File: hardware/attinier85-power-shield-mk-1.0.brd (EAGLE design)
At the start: 36 x 25 mm, 6 parts, among them Q1 2N7000, U1 ATTINIEST85_SHIELD

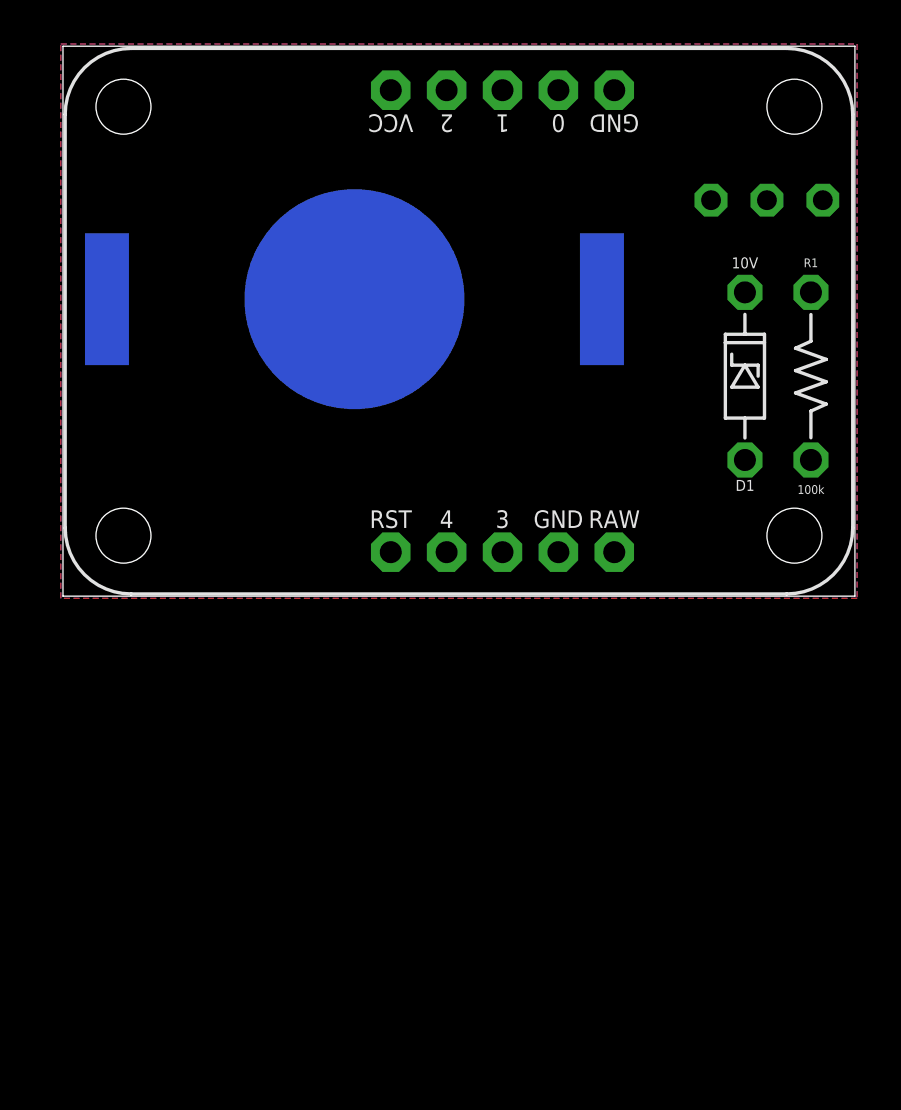
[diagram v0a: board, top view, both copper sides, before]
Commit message: renaming parts
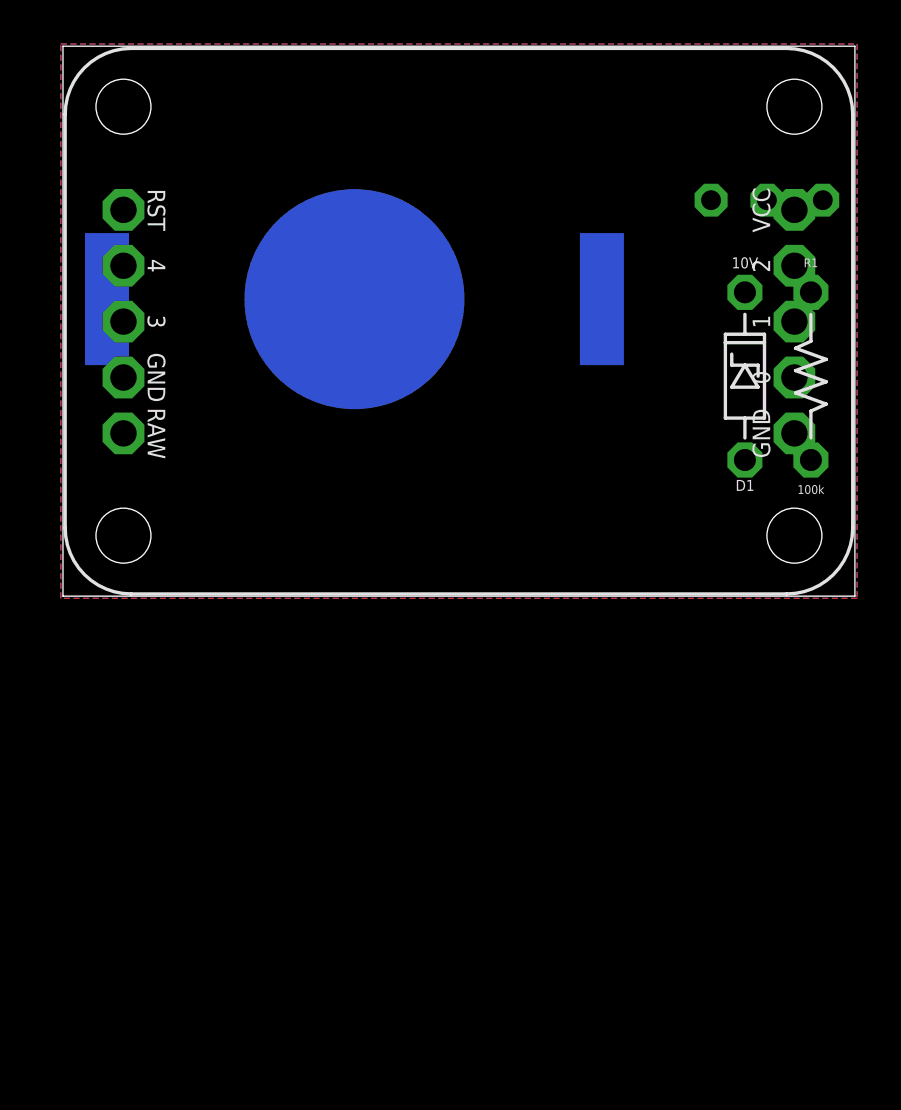
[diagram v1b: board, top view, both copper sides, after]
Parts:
- U1: value ATTINIEST85_SHIELD -> ATTINIER85_SHIELDV2; device A_butts:ATTINIEST85_SHIELD -> A_butts:ATTINIER85_SHIELD_V2
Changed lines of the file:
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@@
 <attribute name="DESIGNER" value="Nobody" x="13.97" y="-1.27" size="1.778" layer="27" display="off"/>
 </element>
-<element name="U1" library="A_butts" package="ATTINIEST85_SHIELD" value="ATTINIEST85_SHIELD" x="18" y="12.5"/>
+<element name="U1" library="A_butts" package="ATTINIER85_SHIELD_V2" value="ATTINIER85_SHIELDV2" x="18" y="12.5"/>
 <element name="BATT" library="A_butts" package="BATTCON_20MM_MINE" value="CR2032" x="13.25" y="13.5" rot="MR90"/>
 <element name="Q1" library="A_butts" package="TO-92-AMMO" value="2N7000" x="32" y="18" rot="MR180"/>

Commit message: shedding useless version
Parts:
- removed BATT: CR2032, A_butts:BATTCON_20MM_MINE
- removed Q1: 2N7000, A_butts:TO-92-AMMO
- removed R1: 100k, A_butts:RESISTOR-AXIAL-PTH-7.62MM
- added D2: 1N5819, A_butts:DIODE-10.16MM
- added IC1: MC34063DIP, A_butts:DIP-08
- added L1: 100 unf, A_butts:INDUCTOR-AXIAL-PTH-10.16MM
- D1: value 10V -> 1N5819; device A_butts:DIODE-ZENNER-7.62MM -> A_butts:DIODE-10.16MM
- moved D1 36.8 mm to (5.50, -16.5), turned to 0 degrees
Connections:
- removed net N$1: BATT.BOTTOM, Q1.1
- removed net N$2: D1.K, Q1.2, R1.P$1
- removed net V_BATT: BATT.TOP@1, R1.P$2
- new net VCC: U1.VCC
- new net VIN: U1.RAW
- net GND: now also U1.GND@1, U1.GND@2; no longer D1.A, Q1.3
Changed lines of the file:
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@@
 </element>
 <element name="U1" library="A_butts" package="ATTINIER85_SHIELD_V2" value="ATTINIER85_SHIELDV2" x="18" y="12.5"/>
-<element name="BATT" library="A_butts" package="BATTCON_20MM_MINE" value="CR2032" x="13.25" y="13.5" rot="MR90"/>
-<element name="Q1" library="A_butts" package="TO-92-AMMO" value="2N7000" x="32" y="18" rot="MR180"/>
-<element name="D1" library="A_butts" package="DIODE-ZENNER-7.62MM" value="10V" x="31" y="10" rot="R90"/>
-<element name="R1" library="A_butts" package="RESISTOR-AXIAL-PTH-7.62MM" value="100k" x="34" y="10" rot="R270"/>
+<element name="IC1" library="A_butts" package="DIP-08" value="MC34063DIP" x="6.5" y="-6"/>
+<element name="L1" library="A_butts" package="INDUCTOR-AXIAL-PTH-10.16MM" value="100 unf" x="6.5" y="-13"/>
+<element name="D1" library="A_butts" package="DIODE-10.16MM" value="1N5819" x="5.5" y="-16.5"/>
+<element name="D2" library="A_butts" package="DIODE-10.16MM" value="1N5819" x="5.5" y="-20"/>
 </elements>
 <signals>
@@
 <vertex x="36.1" y="-0.1"/>
 </polygon>
-<contactref element="Q1" pad="3"/>
-<contactref element="D1" pad="A"/>
+<contactref element="U1" pad="GND@2"/>
+<contactref element="U1" pad="GND@1"/>
+<wire x1="2.75" y1="9.94" x2="33.25" y2="7.4" width="0" layer="19" extent="1-1"/>
 </signal>
-<signal name="N$1">
-<contactref element="BATT" pad="BOTTOM"/>
-<contactref element="Q1" pad="1"/>
-<wire x1="13.25" y1="13.5" x2="29.46" y2="18" width="0" layer="19" extent="16-16"/>
+<signal name="VCC">
+<contactref element="U1" pad="VCC"/>
 </signal>
-<signal name="N$2">
-<contactref element="Q1" pad="2"/>
-<contactref element="D1" pad="K"/>
-<contactref element="R1" pad="P$1"/>
-<wire x1="31" y1="13.81" x2="32" y2="18" width="0" layer="19" extent="1-1"/>
-<wire x1="34" y1="13.81" x2="31" y2="13.81" width="0" layer="19" extent="1-1"/>
-</signal>
-<signal name="V_BATT">
-<contactref element="BATT" pad="TOP@1"/>
-<contactref element="R1" pad="P$2"/>
-<wire x1="24.5" y1="13.5" x2="34" y2="6.19" width="0" layer="19" extent="16-16"/>
+<signal name="VIN">
+<contactref element="U1" pad="RAW"/>
 </signal>
 </signals>

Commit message: wooo
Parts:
- removed D2: 1N5819, A_butts:DIODE-10.16MM
- added C1, C2, C3: 22uF, A_butts:E2,5-6
- added C4: 10nF, A_butts:C025-024X044
- added C5: 200pF, A_butts:C025-024X044
- added L2: 22uH, A_butts:INDUCTOR-AXIAL-PTH-10.16MM
- added R1: 5k, A_butts:RESISTOR-AXIAL-PTH-6.35MM
- added R2: 12.76k, A_butts:RESISTOR-AXIAL-PTH-6.35MM
- added R3: 37.24k, A_butts:RESISTOR-AXIAL-PTH-6.35MM
- IC1: value MC34063DIP -> CS5171; device A_butts:DIP-08 -> A_butts:SO08
- L1: value 100 unf -> 22uH
- moved D1 36.9 mm to (23.0, 16.0), turned to 90 degrees
- moved L1 19.3 mm to (18.0, 2.50)
- moved IC1 18.6 mm to (8.00, 12.5), turned to 180 degrees
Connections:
- new net N$1: C4.2, R1.P$1
- new net N$3: C4.1, C5.1, IC1.1
- new net N$4: IC1.2, R2.P$1, R3.P$1
- new net N$6: C2.+, L1.P$2
- new net N$7: C2.-, D1.A, L2.P$2
- net GND: now also C1.-, C3.-, C5.2, IC1.6, IC1.7, L2.P$1, R1.P$2, R2.P$2
- net VCC: now also C3.+, D1.C, R3.P$2
- net VIN: now also C1.+, IC1.5, L1.P$1
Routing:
- net GND: track 0.00 -> 32.3 mm, vias 0 -> 1
- net VCC: track 0.00 -> 21.3 mm
- net VIN: track 0.00 -> 14.7 mm
- net N$7: track 0.00 -> 9.68 mm
- net N$4: track 0.00 -> 8.43 mm
- net N$3: track 0.00 -> 5.48 mm
- net N$6: track 0.00 -> 5.22 mm
- net N$1: track 0.00 -> 3.16 mm
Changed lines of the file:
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@@
 <setting verticaltext="up"/>
 </settings>
-<grid distance="0.5" unitdist="mm" unit="mm" style="lines" multiple="2" display="yes" altdistance="1" altunitdist="mil" altunit="mil"/>
+<grid distance="0.1" unitdist="mm" unit="mm" style="lines" multiple="5" display="yes" altdistance="1" altunitdist="mil" altunit="mil"/>
 <layers>
 <layer number="1" name="Top" color="4" fill="1" visible="yes" active="yes"/>
@@
 <attribute name="DESIGNER" value="Nobody" x="13.97" y="-1.27" size="1.778" layer="27" display="off"/>
 </element>
-<element name="U1" library="A_butts" package="ATTINIER85_SHIELD_V2" value="ATTINIER85_SHIELDV2" x="18" y="12.5"/>
-<element name="IC1" library="A_butts" package="DIP-08" value="MC34063DIP" x="6.5" y="-6"/>
-<element name="L1" library="A_butts" package="INDUCTOR-AXIAL-PTH-10.16MM" value="100 unf" x="6.5" y="-13"/>
-<element name="D1" library="A_butts" package="DIODE-10.16MM" value="1N5819" x="5.5" y="-16.5"/>
-<element name="D2" library="A_butts" package="DIODE-10.16MM" value="1N5819" x="5.5" y="-20"/>
+<element name="U1" library="A_butts" package="ATTINIER85_SHIELD_V2" value="ATTINIER85_SHIELDV2" x="18" y="12.5" locked="yes"/>
+<element name="L1" library="A_butts" package="INDUCTOR-AXIAL-PTH-10.16MM" value="22uH" x="18" y="2.5"/>
+<element name="D1" library="A_butts" package="DIODE-10.16MM" value="1N5819" x="23" y="16" rot="R90"/>
+<element name="C1" library="A_butts" package="E2,5-6" value="22uF" x="8" y="4.5" smashed="yes" rot="R270">
+<attribute name="NAME" x="8" y="7.478" size="0.5" layer="25" font="vector" ratio="12" align="bottom-center"/>
+<attribute name="VALUE" x="8" y="1.522" size="0.5" layer="27" font="vector" ratio="12" align="top-center"/>
+</element>
+<element name="C2" library="A_butts" package="E2,5-6" value="22uF" x="28" y="4.5" smashed="yes" rot="R90">
+<attribute name="NAME" x="28" y="7.478" size="0.5" layer="25" font="vector" ratio="12" align="bottom-center"/>
+<attribute name="VALUE" x="28" y="1.522" size="0.5" layer="27" font="vector" ratio="12" align="top-center"/>
+</element>
+<element name="IC1" library="A_butts" package="SO08" value="CS5171" x="8" y="12.5" rot="R180"/>
+<element name="C4" library="A_butts" package="C025-024X044" value="10nF" x="14" y="15.5"/>
+<element name="R1" library="A_butts" package="RESISTOR-AXIAL-PTH-6.35MM" value="5k" x="10.5" y="18" rot="R180"/>
+<element name="R2" library="A_butts" package="RESISTOR-AXIAL-PTH-6.35MM" value="12.76k" x="10.5" y="23"/>
+<element name="R3" library="A_butts" package="RESISTOR-AXIAL-PTH-6.35MM" value="37.24k" x="10.5" y="20.5"/>
+<element name="C3" library="A_butts" package="E2,5-6" value="22uF" x="28" y="21"/>
+<element name="C5" library="A_butts" package="C025-024X044" value="200pF" x="14" y="13"/>
+<element name="L2" library="A_butts" package="INDUCTOR-AXIAL-PTH-10.16MM" value="22uH" x="18" y="6.5"/>
 </elements>
 <signals>
 <signal name="GND">
 <polygon width="0.1524" layer="1">
+<vertex x="36.1" y="-0.1"/>
 <vertex x="-0.1" y="-0.1"/>
-<vertex x="-0.1" y="25.1"/>
+<vertex x="-0.1" y="11.5"/>
+<vertex x="5" y="11.5"/>
+<vertex x="5" y="8.1"/>
+<vertex x="11" y="8.1"/>
+<vertex x="11" y="11"/>
+<vertex x="17" y="11"/>
+<vertex x="17" y="25.1"/>
 <vertex x="36.1" y="25.1"/>
-<vertex x="36.1" y="-0.1"/>
-</polygon>
-<polygon width="0.1524" layer="16">
-<vertex x="-0.1" y="-0.1"/>
-<vertex x="-0.1" y="25.1"/>
-<vertex x="36.1" y="25.1"/>
-<vertex x="36.1" y="-0.1"/>
 </polygon>
 <contactref element="U1" pad="GND@2"/>
 <contactref element="U1" pad="GND@1"/>
-<wire x1="2.75" y1="9.94" x2="33.25" y2="7.4" width="0" layer="19" extent="1-1"/>
+<contactref element="R1" pad="P$2"/>
+<contactref element="C5" pad="2"/>
+<contactref element="R2" pad="P$2"/>
+<contactref element="IC1" pad="7"/>
+<contactref element="IC1" pad="6"/>
+<contactref element="C1" pad="-"/>
+<contactref element="L2" pad="P$1"/>
+<contactref element="C3" pad="-"/>
+<polygon width="0.1524" layer="16">
+<vertex x="36.1" y="-0.1"/>
+<vertex x="-0.1" y="-0.1"/>
+<vertex x="-0.1" y="11.5"/>
+<vertex x="5" y="11.5"/>
+<vertex x="5" y="8.1"/>
+<vertex x="11" y="8.1"/>
+<vertex x="11" y="11"/>
+<vertex x="17" y="11"/>
+<vertex x="17" y="25.1"/>
+<vertex x="36.1" y="25.1"/>
+</polygon>
+<wire x1="8.635" y1="9.8838" x2="8.635" y2="7.7" width="1.27" layer="1"/>
+<wire x1="7.365" y1="9.8838" x2="7.365" y2="12.5" width="0.6" layer="1"/>
+<wire x1="7.365" y1="12.5" x2="5.9" y2="12.5" width="0.6" layer="1"/>
+<wire x1="5.9" y1="12.5" x2="4.5" y2="11.1" width="0.6" layer="1"/>
+<wire x1="4.5" y1="11.1" x2="4.5" y2="10.9" width="0.6" layer="1"/>
+<wire x1="7.365" y1="12.5" x2="9.6" y2="12.5" width="0.6" layer="16"/>
+<wire x1="9.6" y1="12.5" x2="11.3" y2="14.2" width="0.6" layer="16"/>
+<wire x1="11.3" y1="14.2" x2="14.07" y2="14.2" width="0.6" layer="16"/>
+<wire x1="14.07" y1="14.2" x2="15.27" y2="13" width="0.6" layer="16"/>
+<wire x1="7.325" y1="18" x2="9.8" y2="18" width="0.6" layer="16"/>
+<wire x1="9.8" y1="18" x2="11.3" y2="16.5" width="0.6" layer="16"/>
+<via x="7.365" y="12.5" extent="1-16" drill="0.3302"/>
+<wire x1="11.3" y1="14.2" x2="11.3" y2="16.5" width="0.6" layer="16"/>
+<wire x1="9.8" y1="18" x2="9.8" y2="21.3" width="0.6" layer="16"/>
+<wire x1="9.8" y1="21.3" x2="11.5" y2="23" width="0.6" layer="16"/>
+<wire x1="11.5" y1="23" x2="13.675" y2="23" width="0.6" layer="16"/>
 </signal>
 <signal name="VCC">
 <contactref element="U1" pad="VCC"/>
+<contactref element="R3" pad="P$2"/>
+<contactref element="D1" pad="C"/>
+<contactref element="C3" pad="+"/>
+<wire x1="23" y1="21.08" x2="14.255" y2="21.08" width="0.6" layer="1"/>
+<wire x1="14.255" y1="21.08" x2="13.675" y2="20.5" width="0.6" layer="1"/>
+<wire x1="23" y1="21.08" x2="26.65" y2="21.08" width="0.6" layer="1"/>
+<wire x1="26.65" y1="21.08" x2="26.73" y2="21" width="0.6" layer="1"/>
+<wire x1="33.25" y1="17.56" x2="30.17" y2="17.56" width="0.6" layer="1"/>
+<wire x1="30.17" y1="17.56" x2="26.73" y2="21" width="0.6" layer="1"/>
 </signal>
 <signal name="VIN">
 <contactref element="U1" pad="RAW"/>
+<contactref element="C1" pad="+"/>
+<contactref element="IC1" pad="5"/>
+<contactref element="L1" pad="P$1"/>
+<wire x1="2.75" y1="7.4" x2="6.095" y2="7.4" width="0.6" layer="1"/>
+<wire x1="6.095" y1="7.4" x2="6.095" y2="9.8838" width="0.6" layer="1"/>
+<wire x1="6.095" y1="7.4" x2="7.725" y2="5.77" width="0.6" layer="1"/>
+<wire x1="7.725" y1="5.77" x2="8" y2="5.77" width="0.6" layer="1"/>
+<wire x1="8" y1="5.77" x2="9.65" y2="5.77" width="0.6" layer="1"/>
+<wire x1="9.65" y1="5.77" x2="12.92" y2="2.5" width="0.6" layer="1"/>
+</signal>
+<signal name="N$1">
+<contactref element="C4" pad="2"/>
+<contactref element="R1" pad="P$1"/>
+<wire x1="15.27" y1="15.5" x2="15.27" y2="16.405" width="0.6" layer="1"/>
+<wire x1="15.27" y1="16.405" x2="13.675" y2="18" width="0.6" layer="1"/>
+</signal>
+<signal name="N$3">
+<contactref element="C5" pad="1"/>
+<contactref element="IC1" pad="1"/>
+<contactref element="C4" pad="1"/>
+<wire x1="12.73" y1="13" x2="12.73" y2="15.5" width="0.6" layer="1"/>
+<wire x1="9.905" y1="15.1162" x2="12.3462" y2="15.1162" width="0.6" layer="1"/>
+<wire x1="12.3462" y1="15.1162" x2="12.73" y2="15.5" width="0.6" layer="1"/>
+</signal>
+<signal name="N$4">
+<contactref element="IC1" pad="2"/>
+<contactref element="R2" pad="P$1"/>
+<contactref element="R3" pad="P$1"/>
+<wire x1="8.635" y1="15.1162" x2="8.635" y2="19.19" width="0.6" layer="1"/>
+<wire x1="8.635" y1="19.19" x2="7.325" y2="20.5" width="0.6" layer="1"/>
+<wire x1="7.325" y1="20.5" x2="7.325" y2="23" width="0.6" layer="1"/>
+</signal>
+<signal name="N$6">
+<contactref element="L1" pad="P$2"/>
+<contactref element="C2" pad="+"/>
+<wire x1="28" y1="3.23" x2="23.81" y2="3.23" width="0.6" layer="1"/>
+<wire x1="23.81" y1="3.23" x2="23.08" y2="2.5" width="0.6" layer="1"/>
+</signal>
+<signal name="N$7">
+<contactref element="L2" pad="P$2"/>
+<contactref element="C2" pad="-"/>
+<contactref element="D1" pad="A"/>
+<wire x1="23" y1="10.92" x2="23" y2="6.58" width="0.6" layer="1"/>
+<wire x1="23" y1="6.58" x2="23.08" y2="6.5" width="0.6" layer="1"/>
+<wire x1="28" y1="5.77" x2="23.81" y2="5.77" width="0.6" layer="1"/>
+<wire x1="23.81" y1="5.77" x2="23.08" y2="6.5" width="0.6" layer="1"/>
 </signal>
 </signals>
